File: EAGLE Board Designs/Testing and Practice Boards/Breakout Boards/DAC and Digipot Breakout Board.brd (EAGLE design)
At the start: 160 x 101.3 mm, 34 parts, among them J1 JUMPER.1, X1 CONNECTOR-4NANO-FIT-VERTICAL-4

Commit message: more board work
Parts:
- moved U$7 107.2 mm to (4.45, 35.6), turned to 180 degrees
- moved U$6 104.4 mm to (8.89, 35.6), turned to 180 degrees
- moved U$8 96.7 mm to (14.0, 35.6), turned to 180 degrees
- moved U$9 90.7 mm to (19.1, 35.6), turned to 180 degrees
- moved JP2 74.0 mm to (11.4, 41.9), turned to 0 degrees
- moved JP3 6.84 mm to (80.0, 86.4)
- moved U$20 6.27 mm to (11.7, 51.3), turned to 0 degrees
- moved C3 4.51 mm to (17.4, 51.2), turned to 270 degrees
- moved C4 4.40 mm to (15.2, 51.2), turned to 270 degrees
- moved C7 1.63 mm to (6.86, 48.8)
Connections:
- net 5V_DAC_OUTPUT_A: now also JP2.2; no longer JP2.1
- net 5V_DAC_OUTPUT_B: now also JP2.1; no longer JP2.2
- net CS_2: now also U$2.D5; no longer U$2.D8(TX3)
- net CS_3: now also U$2.D12; no longer U$2.D7(RX3)
- net GAIN: now also U$2.D6; no longer U$2.D9(RX2)
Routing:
- net SCLK: track 33.4 -> 74.0 mm
- net GND: track 123.6 -> 160.4 mm
- net +5V: track 12.8 -> 47.4 mm
- net MOSI: track 52.1 -> 80.1 mm, vias 0 -> 1
- net +3V3: track 17.3 -> 44.3 mm
- net 5V_DAC_OUTPUT_D: track 0.00 -> 15.5 mm
- net 5V_DAC_OUTPUT_B: track 0.00 -> 15.5 mm
- net GAIN: track 0.00 -> 13.9 mm
- net 5V_DAC_OUTPUT_A: track 0.00 -> 13.9 mm
- net 5V_DAC_OUTPUT_C: track 0.00 -> 13.7 mm
- net CS_2: track 0.00 -> 11.0 mm
- net N$4: track 2.66 -> 1.73 mm

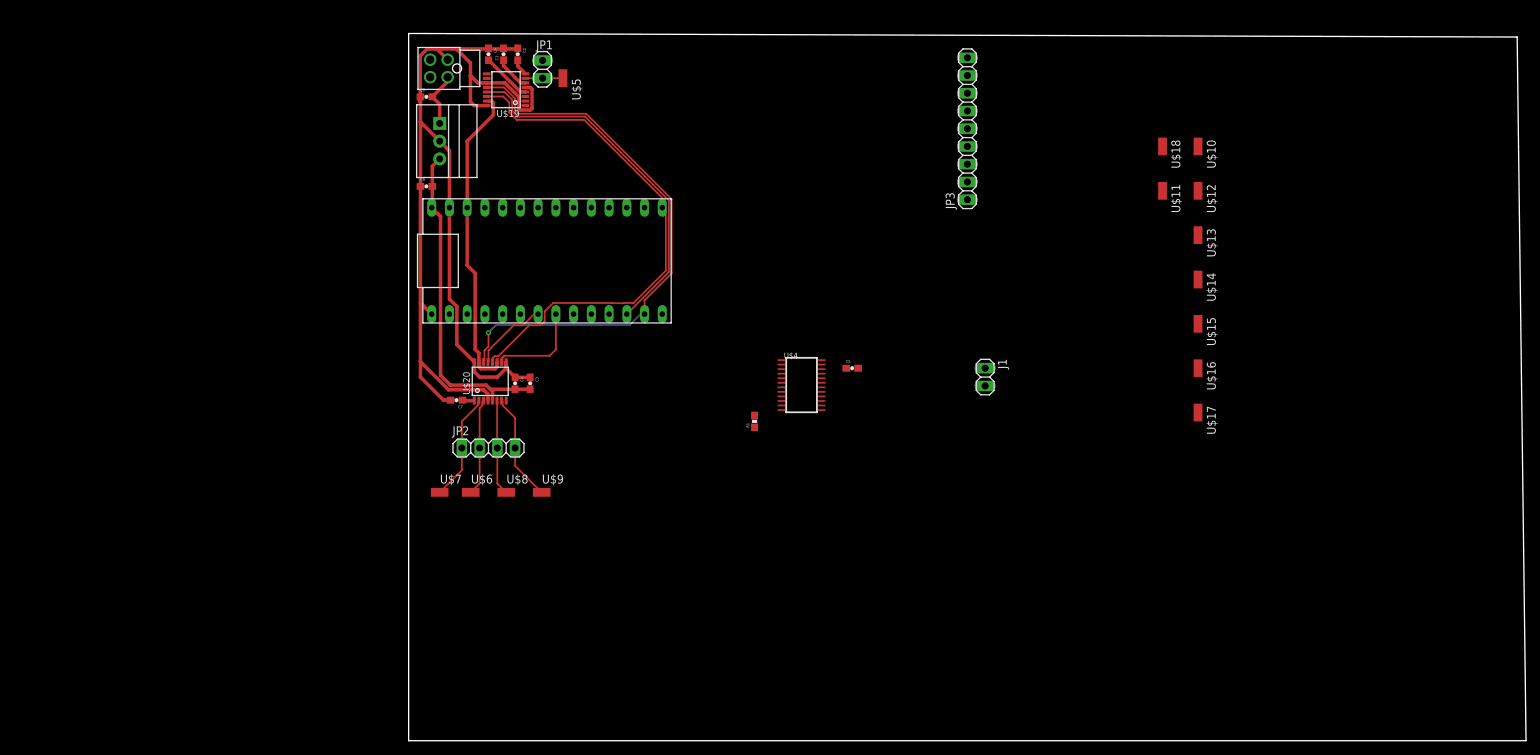
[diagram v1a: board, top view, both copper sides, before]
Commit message: Finish routing board with some bottom traces
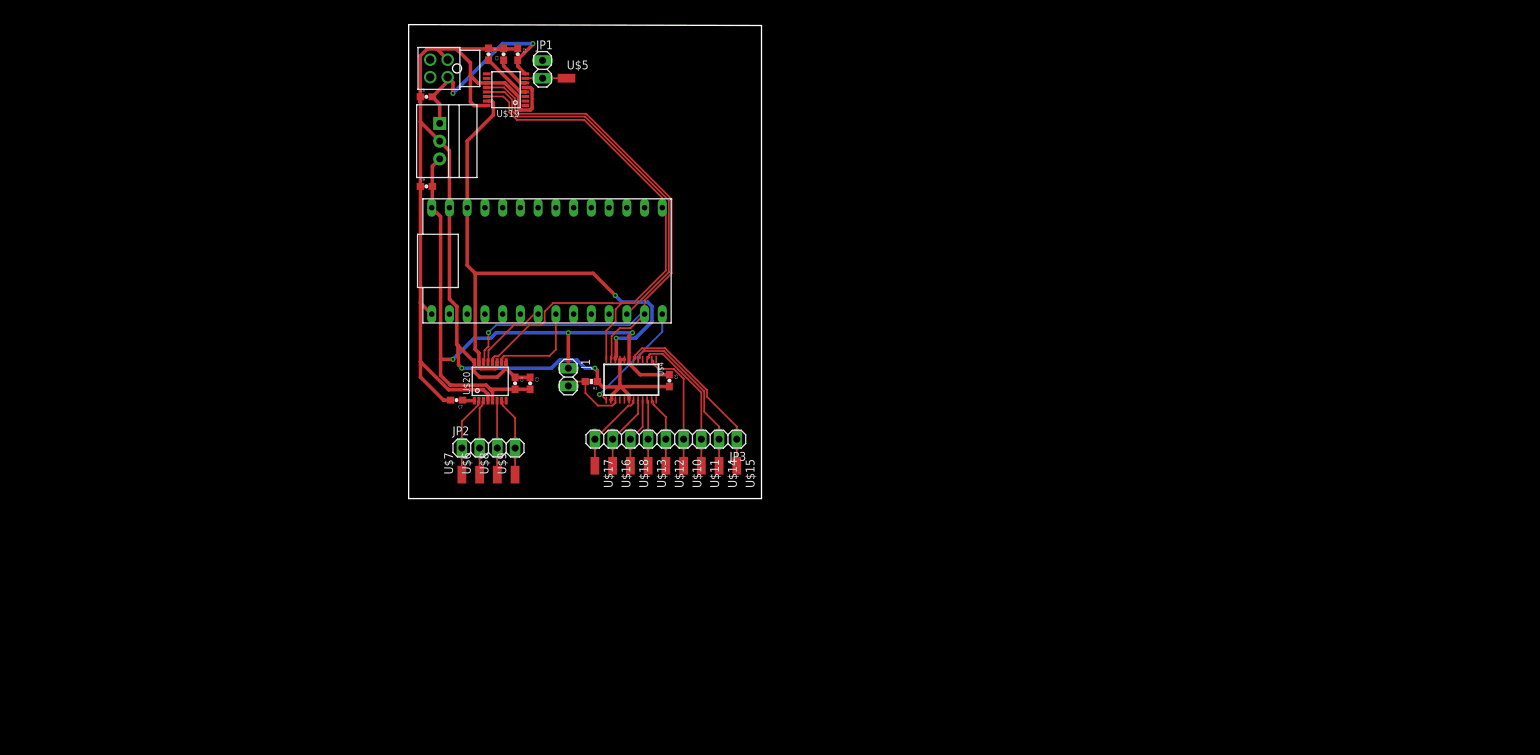
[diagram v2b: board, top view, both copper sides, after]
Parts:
- moved U$18 88.9 mm to (31.8, 39.4)
- moved U$10 86.7 mm to (39.4, 39.4)
- moved U$17 86.7 mm to (26.7, 39.4)
- moved U$12 85.8 mm to (36.8, 39.4)
- moved U$13 85.4 mm to (34.3, 39.4)
- moved U$16 85.0 mm to (29.2, 39.4)
- moved U$11 76.9 mm to (41.9, 39.4)
- moved U$14 73.6 mm to (44.5, 39.4)
- moved U$15 69.1 mm to (47.0, 39.4)
- moved JP3 60.2 mm to (38.1, 43.2), turned to 180 degrees
- moved J1 59.7 mm to (22.9, 52.1)
- moved C5 26.2 mm to (37.3, 51.6), turned to 270 degrees
- moved U$4 24.4 mm to (31.9, 51.7), turned to 270 degrees
- moved R1 24.1 mm to (26.2, 51.4), turned to 180 degrees
- moved U$9 4.58 mm to (15.2, 38.1), turned to 270 degrees
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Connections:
- removed net SDI: U$4.11
- net MOSI: now also U$4.11
- net POTEN_A1: now also JP3.4; no longer JP3.3
- net POTEN_A3: now also JP3.2; no longer JP3.1
- net POTEN_A4: now also JP3.8; no longer JP3.7
- net POTEN_B4: now also JP3.7; no longer JP3.9
- net POTEN_W1: now also JP3.3; no longer JP3.4
- net POTEN_W3: now also JP3.1; no longer JP3.2
- net POTEN_W4: now also JP3.9; no longer JP3.8
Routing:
- net GND: track 160.4 -> 208.7 mm, vias 0 -> 2
- net +5V: track 47.4 -> 92.6 mm, vias 0 -> 3
- net +3V3: track 44.3 -> 83.0 mm, vias 0 -> 2
- net POTEN_W3: track 0.00 -> 26.5 mm
- net POTEN_A3: track 0.00 -> 24.1 mm
- net POTEN_W1: track 0.00 -> 21.1 mm
- net +12V: track 10.4 -> 30.6 mm, vias 0 -> 2
- net POTEN_A1: track 0.00 -> 18.4 mm
- net CS_3: track 0.00 -> 16.5 mm, vias 0 -> 1
- net POTEN_W4: track 0.00 -> 11.9 mm
- net POTEN_A4: track 0.00 -> 10.9 mm
- net POTEN_A2: track 0.00 -> 10.3 mm
- net POTEN_B4: track 0.00 -> 10.1 mm
- net N$2: track 0.00 -> 9.97 mm
- net POTEN_W2: track 0.00 -> 9.48 mm
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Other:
- board size 160 x 101.3 mm -> 50.5 x 67.9 mm

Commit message: all my homies hate drc
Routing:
- net GND: track 208.7 -> 205.3 mm
- net N$2: track 9.97 -> 10.6 mm
- net GAIN: track 13.9 -> 13.4 mm

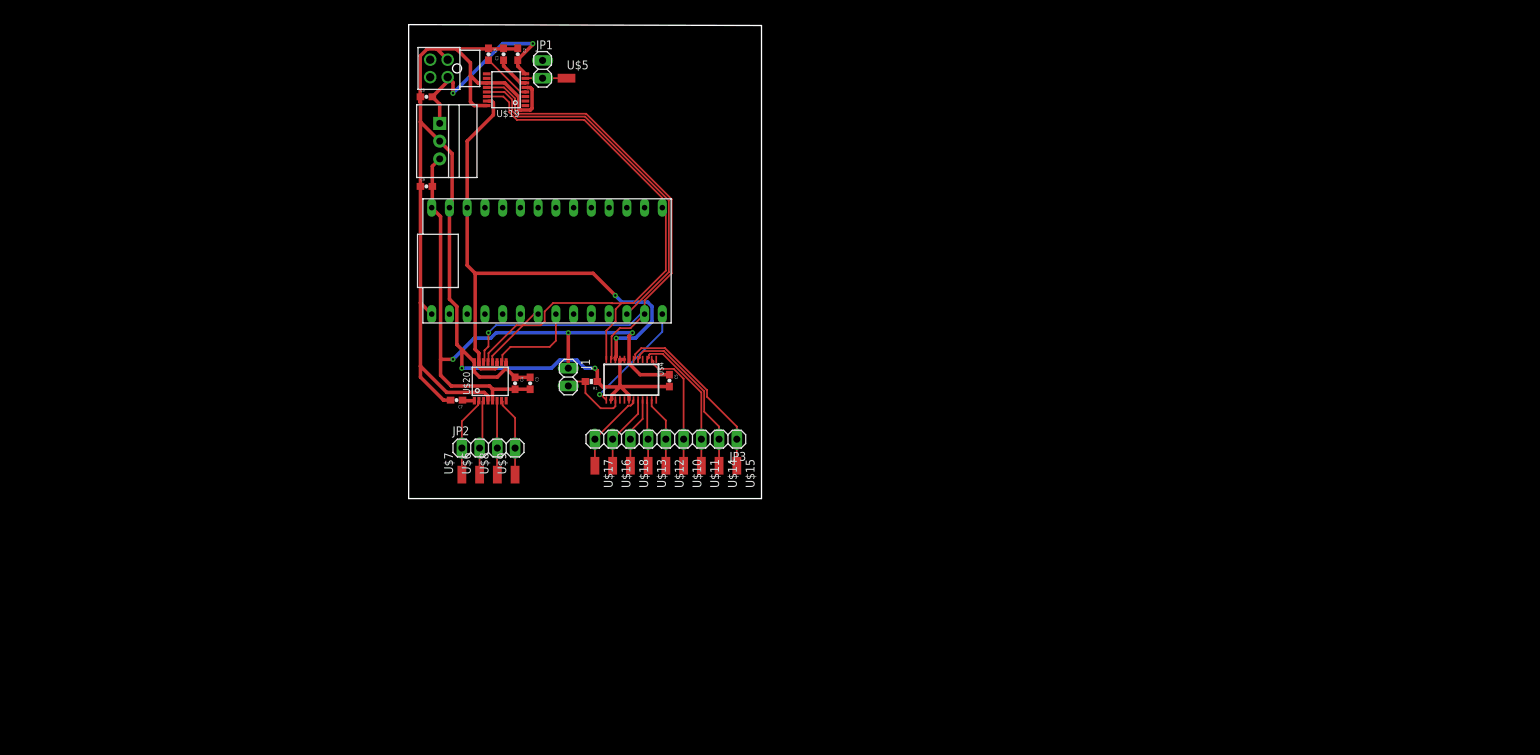
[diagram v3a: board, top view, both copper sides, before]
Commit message: restarted board to match on campus drc
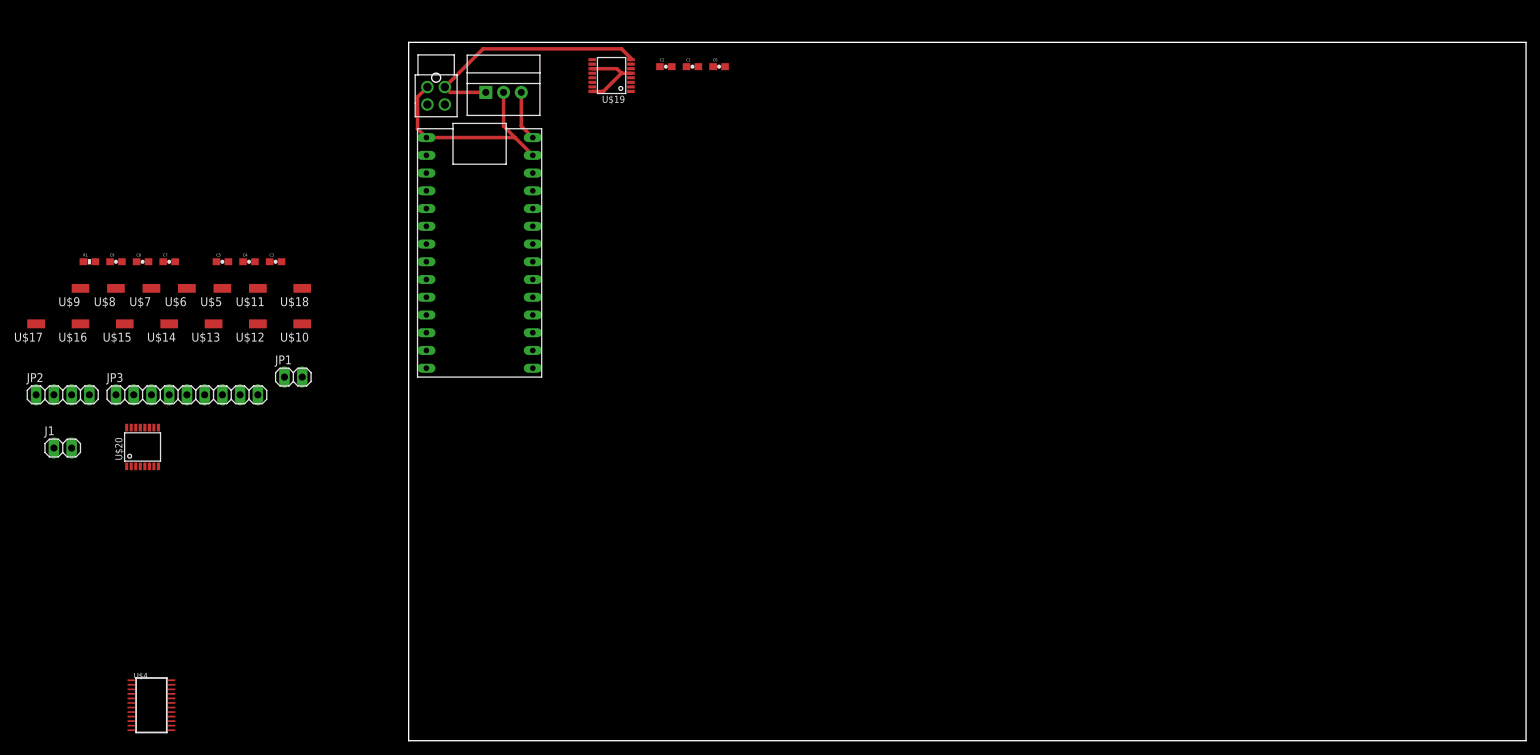
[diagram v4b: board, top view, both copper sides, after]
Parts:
- moved U$15 90.0 mm to (-40.6, 59.7), turned to 0 degrees
- moved U$4 83.0 mm to (-36.8, 5.08), turned to 0 degrees
- moved U$17 82.5 mm to (-53.3, 59.7), turned to 0 degrees
- moved U$14 81.3 mm to (-34.3, 59.7), turned to 0 degrees
- moved U$16 78.9 mm to (-47.0, 59.7), turned to 0 degrees
- moved R1 73.9 mm to (-45.7, 68.6), turned to 0 degrees
- moved J1 73.1 mm to (-49.5, 41.9), turned to 0 degrees
- moved JP3 71.4 mm to (-33.0, 49.5), turned to 0 degrees
- moved U$11 68.4 mm to (-21.6, 64.8), turned to 0 degrees
- moved U$9 67.7 mm to (-47.0, 64.8), turned to 0 degrees
- moved C5 66.2 mm to (-26.7, 68.6), turned to 0 degrees
- moved U$13 65.5 mm to (-27.9, 59.7), turned to 0 degrees
- moved U$12 61.9 mm to (-21.6, 59.7), turned to 0 degrees
- moved JP2 61.4 mm to (-49.5, 49.5)
- moved U$8 60.8 mm to (-41.9, 64.8), turned to 0 degrees
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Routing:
- net GND: track 205.3 -> 42.9 mm, vias 2 -> 0
- net MOSI: track 89.5 -> 0.00 mm, vias 1 -> 0
- net +5V: track 92.5 -> 7.16 mm, vias 3 -> 0
- net SCLK: track 83.2 -> 0.00 mm
- net +3V3: track 83.0 -> 0.00 mm, vias 2 -> 0
- net CS_1: track 52.2 -> 0.00 mm
- net POTEN_W3: track 26.6 -> 0.00 mm
- net POTEN_A3: track 24.1 -> 0.00 mm
- net POTEN_W1: track 21.1 -> 0.00 mm
- net POTEN_A1: track 18.4 -> 0.00 mm
- net CS_3: track 16.5 -> 0.00 mm, vias 1 -> 0
- net GAIN: track 13.4 -> 0.00 mm
- net POTEN_W4: track 11.9 -> 0.00 mm
- net 5V_DAC_OUTPUT_B: track 11.6 -> 0.00 mm
- net 5V_DAC_OUTPUT_D: track 11.4 -> 0.00 mm
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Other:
- board size 50.5 x 67.9 mm -> 160 x 100 mm

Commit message: redo board with on campus 2 layer drc
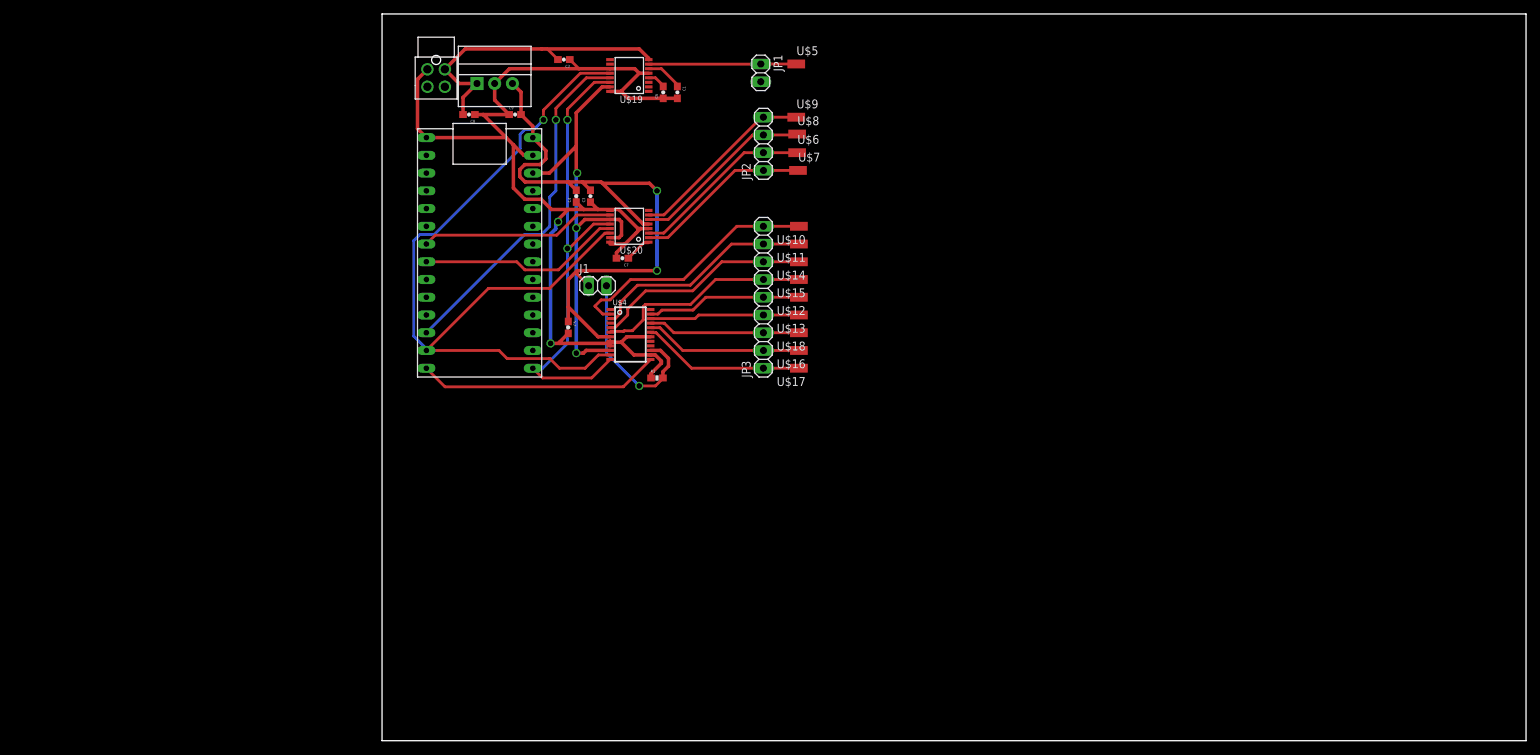
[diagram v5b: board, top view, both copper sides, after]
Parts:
- moved U$17 109.4 mm to (55.9, 53.3)
- moved JP2 106.6 mm to (50.8, 85.5), turned to 90 degrees
- moved U$9 105.4 mm to (55.5, 89.3), turned to 180 degrees
- moved U$16 102.9 mm to (55.9, 55.9)
- moved U$8 100.0 mm to (55.6, 86.9), turned to 180 degrees
- moved U$15 96.7 mm to (55.9, 66.0)
- moved U$7 94.1 mm to (55.8, 81.7), turned to 180 degrees
- moved U$14 90.6 mm to (55.9, 68.6)
- moved U$6 89.5 mm to (55.6, 84.2), turned to 180 degrees
- moved U$5 88.2 mm to (55.5, 96.9), turned to 180 degrees
- moved U$4 86.7 mm to (31.8, 58.2)
- moved JP3 84.8 mm to (50.8, 62.2), turned to 90 degrees
- moved U$13 83.8 mm to (55.9, 61.0)
- moved R1 83.0 mm to (35.6, 51.9)
- moved J1 80.0 mm to (27.1, 65.2)
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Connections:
- net CS_2: now also U$2.D6; no longer U$2.D5
- net GAIN: now also U$2.D5; no longer U$2.D6
- net POTEN_A1: now also JP3.9; no longer JP3.4
- net POTEN_A3: now also JP3.7; no longer JP3.2
- net POTEN_A4: now also JP3.2; no longer JP3.8
- net POTEN_B4: now also JP3.3; no longer JP3.7
- net POTEN_W1: now also JP3.8; no longer JP3.3
- net POTEN_W2: now also JP3.4; no longer JP3.6
- net POTEN_W3: now also JP3.6; no longer JP3.1
- net POTEN_W4: now also JP3.1; no longer JP3.9
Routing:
- net GND: track 42.9 -> 167.5 mm, vias 0 -> 2
- net MOSI: track 0.00 -> 117.9 mm, vias 0 -> 1
- net +5V: track 7.16 -> 92.3 mm, vias 0 -> 2
- net SCLK: track 0.00 -> 67.9 mm, vias 0 -> 2
- net +3V3: track 0.00 -> 64.5 mm, vias 0 -> 3
- net CS_1: track 0.00 -> 50.8 mm, vias 0 -> 1
- net POTEN_A1: track 0.00 -> 36.6 mm
- net CS_3: track 0.00 -> 34.8 mm
- net POTEN_W1: track 0.00 -> 32.4 mm
- net POTEN_A3: track 0.00 -> 31.5 mm
- net POTEN_W3: track 0.00 -> 31.3 mm
- net CS_2: track 0.00 -> 29.2 mm
- net GAIN: track 0.00 -> 28.0 mm
- net 5V_DAC_OUTPUT_D: track 0.00 -> 26.9 mm
- net N$2: track 0.00 -> 26.4 mm, vias 0 -> 1
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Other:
- board size 160 x 100 mm -> 163.8 x 104.1 mm

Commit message: fix according to ethan suggestions
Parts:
- moved C8 17.8 mm to (-9.14, 89.7)
- moved C9 17.8 mm to (-2.54, 89.7)
- moved U$1 17.8 mm to (-5.46, 94.1)
- moved X1 17.8 mm to (-13.8, 96.1)
- moved JP1 2.54 mm to (50.5, 98.2), turned to 90 degrees
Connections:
- net GND: now also JP1.2
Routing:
- net GND: track 167.5 -> 279.2 mm
- net +12V: track 44.8 -> 62.6 mm
- net +5V: track 92.3 -> 109.1 mm
- net POTEN_A1: track 36.6 -> 35.4 mm
- net MOSI: track 117.9 -> 117.2 mm
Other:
- board size 163.8 x 104.1 mm -> 78.6 x 54.7 mm
